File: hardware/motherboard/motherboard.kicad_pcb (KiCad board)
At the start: 4 copper layers, 150 x 90 mm, 32 parts, among them J1 Custom_PCIe_x4, J10 Conn_01x50_MountingPin, J11 Conn_01x50_MountingPin, J12 Barrel_Jack_Switch_Pin3Ring, J2 Custom_PCIe_x4, J3 Custom_PCIe_x4, J4 Custom_PCIe_x4, J5 Custom_PCIe_x4, J6 Custom_PCIe_x4, J7 Custom_PCIe_x4, J8 Custom_PCIe_x4, J9 Conn_01x50_MountingPin, U1 74HC138, U2 TMUX1208PW, U3 SN74LV595, U5 74HC138

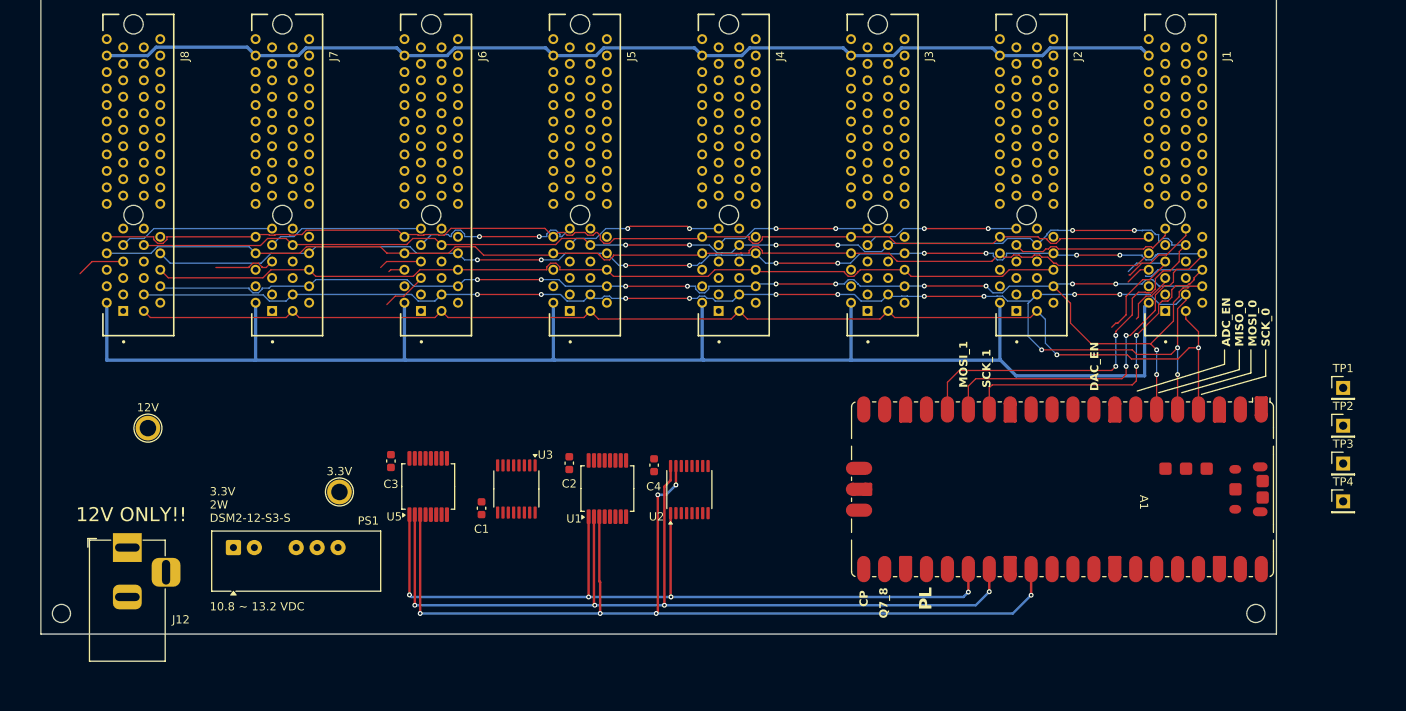
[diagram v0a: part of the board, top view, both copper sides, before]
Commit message: Motherboard: protected power input, K7805 switcher, working 3V3_EN interlock
Rework the motherboard power tree from the barrel jack to the 3.3 V rail.
Design rationale and verification are recorded in hardware/motherboard/POWER.md.

Input protection (new):
- F1 PPTC 1.5 A hold / 3 A trip (1812L150/24MR) -> D2 SMBJ13A TVS -> Q1 AO3407A
  P-FET reverse-polarity, in that order so a surge or reversed jack crowbars
  through the fuse.
- Q1 is drain-to-supply / source-to-load; source-to-supply passes reverse
  current through the body diode and fails silently.
- AO3407A (Vgs +/-20 V) replaces AO3401A (+/-12 V), which sat at its absolute
  maximum on a 12 V rail and needed a gate zener conducting continuously.
- +12 V now actually reaches J1-J8 pin A30; it was previously an orphan net
  with no source.

Regulation:
- U8 L7805 -> K7805-500R3 switching module, pin-compatible with LM78xx.
  Cuts 12->5 V loss from ~1.5 W to ~0.15 W. TRACO TSR-1 symbol/footprint match
  the datasheet layout (3 x 1.00 mm holes, 2.54 mm pitch).
- Datasheet-required caps added: C5 10 uF/50 V at the input, C6 22 uF at the
  output, C7 220 uF electrolytic bulk for load steps and hot-plug damping.

3V3_EN interlock (was inert):
- R7 100k -> 10k, R8 100k -> 4.7k with its far end moved from the Pico's own
  3V3 output (pin 36) to the board +3.3 V rail. As wired it was a bootstrap
  divider off the regulator's own output that enabled in every case.
- Verified against RT6150A/B DS6150A/B-06: EN logic-low max 0.4 V, logic-high
  min 1.2 V. Board rail dead -> 0.146 V (off); rail up -> 2.32 V (on).

Also:
- U1/U5 SN74LVC138APWR -> SN74HC138PWR: 8x cheaper, ~50k stock vs 669, and
  the decoders are static during a transfer (address then enable, then SPI).
  Footprint corrected SSOP-16 -> TSSOP-16, matching the PW part and U2/U3.
- Capacitors standardised on 0805 (C8 stays 1210 for DC-bias reasons).
- Footprints assigned to F1/R1/R6/R7/R8; LCSC part numbers recorded in POWER.md.
- .gitignore: padne output, Ki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
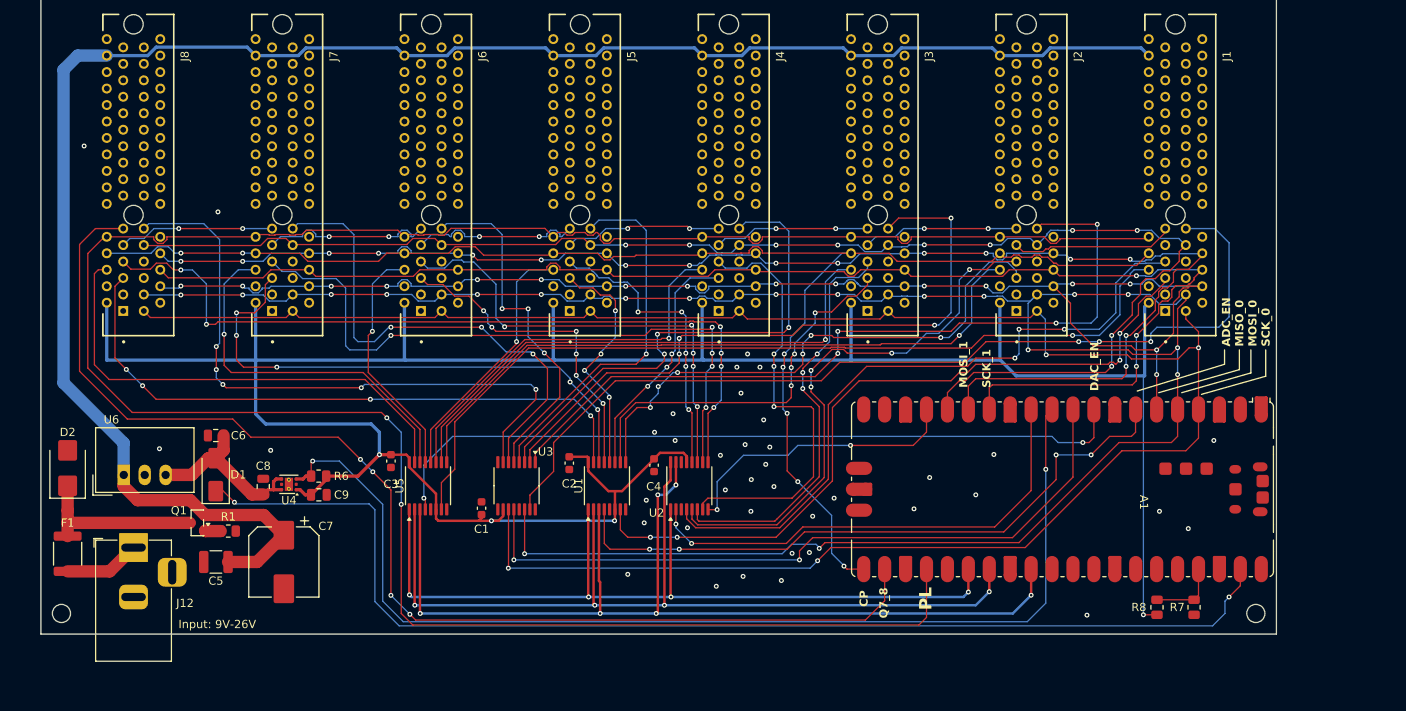
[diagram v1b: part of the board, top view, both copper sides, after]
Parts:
- removed 12V, 3.3V: TestPoint_Plated_Hole_D2.0mm, TestPoint:TestPoint_Plated_Hole_D2.0mm
- removed PS1: DSM2-12-S3-S, Converter_DCDC:Converter_DCDC_XP_POWER-IAxxxxS_THT
- removed TP1, TP2, TP3, TP4: TestPoint, Connector_PinHeader_2.54mm:PinHeader_1x01_P2.54mm_Vertical
- added C5: 10uF, Capacitor_SMD:C_1210_3225Metric, F.Cu at (103.8, 123.8)
- added C6: 22uF, Capacitor_SMD:C_0805_2012Metric, F.Cu at (103.7, 108.4)
- added C7: 220uF, Capacitor_SMD:CP_Elec_8x10, F.Cu at (112.0, 123.8)
- added C8: 10uF, Capacitor_SMD:C_0805_2012Metric, F.Cu at (109.5, 114.6)
- added C9: 10uF, Capacitor_SMD:C_0805_2012Metric, F.Cu at (116.2, 115.6)
- added D1: SS34, Diode_SMD:D_SMA, F.Cu at (103.7, 113.2)
- added D2: SMBJ13A, Diode_SMD:D_SMB, F.Cu at (85.8, 112.3)
- added F1: 1812L150/24MR, Fuse:Fuse_1812_4532Metric, F.Cu at (85.8, 122.8)
- added Q1: AO3407A, Package_TO_SOT_SMD:SOT-23, F.Cu at (101.5, 119.0)
- added R1: 100k, Resistor_SMD:R_0805_2012Metric, F.Cu at (105.2, 120.0)
- added R6: 100k, Resistor_SMD:R_0805_2012Metric, F.Cu at (116.2, 113.3)
- added R7: 10k, Resistor_SMD:R_0805_2012Metric, F.Cu at (222.5, 129.2)
- added R8: 4.7k, Resistor_SMD:R_0805_2012Metric, F.Cu at (218.0, 129.2)
- added U4: LP5912-3.3DRV, Package_SON:WSON-6-1EP_2x2mm_P0.65mm_EP1x1.6mm_ThermalVias, F.Cu at (112.6, 114.3)
- added U6: K7805-500R3, Converter_DCDC:Converter_DCDC_TRACO_TSR-1_THT, F.Cu at (92.6, 113.2)
- J1, J2, J3, J4, J5, J6, J7, J8: value Custom_PCIe_x4 -> PCIE-064-02-F-D-TH
- U1, U5: value 74HC138 -> SN74HC138PWR; footprint Package_SO:SSOP-16_5.3x6.2mm_P0.65mm -> Package_SO:TSSOP-16_4.4x5mm_P0.65mm
- moved J12 0.75 mm to (93.8, 122.0)
- moved U2 0.46 mm to (161.2, 114.5)
- moved U3 0.39 mm to (140.2, 114.5)
- moved U1 0.34 mm to (151.2, 114.5)
- moved U5 0.09 mm to (129.5, 114.5)
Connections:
- A1 pad 11: unconnected-(A1-GPIO8-Pad11) -> PG
- A1 pad 37: unconnected-(A1-3V3_EN-Pad37) -> 3V3_EN
- A1 pad 39: unconnected-(A1-VSYS-Pad39) -> VSYS
- J1 pad B31: GND -> PRSNT
- J12 pad 1: +12V -> VIN_JACK
- J2 pad B31: GND -> unconnected-(J2-~{PRSNT2}-PadB31)
- J4 pad B31: GND -> unconnected-(J4-~{PRSNT2}-PadB31)
- J5 pad B31: GND -> unconnected-(J5-~{PRSNT2}-PadB31)
- J6 pad B31: GND -> unconnected-(J6-~{PRSNT2}-PadB31)
- J7 pad B31: GND -> unconnected-(J7-~{PRSNT2}-PadB31)
- J8 pad B31: GND -> unconnected-(J8-~{PRSNT2}-PadB31)
- U1 pad 6: GND -> +3.3V
- U5 pad 6: GND -> +3.3V
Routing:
- net PL: track 133.7 -> 285.0 mm, vias 0 -> 2
- net Q7_8: track 0.00 -> 144.1 mm, vias 0 -> 4
- net VSYS: track 0.00 -> 142.6 mm, vias 0 -> 2
- net PG: track 0.00 -> 132.6 mm, vias 0 -> 2
- net +3.3V: track 184.9 -> 315.6 mm, vias 0 -> 4
- net XTR_OD_1: track 9.73 -> 113.2 mm, vias 0 -> 3
- net DAC_CS1: track 3.11 -> 106.0 mm, vias 0 -> 1
- net SCK_0: track 149.6 -> 251.2 mm, vias 2 -> 4
- net XTR_OD_2: track 0.00 -> 96.6 mm, vias 0 -> 4
- net MOSI_0: track 171.2 -> 266.5 mm, vias 13 -> 19
- net DAC_EN: track 0.00 -> 92.2 mm, vias 0 -> 2
- net AT8: track 5.86 -> 96.6 mm, vias 0 -> 6
- net +12V: track 132.0 -> 221.6 mm
- net XTR_RCLK: track 0.00 -> 87.0 mm, vias 0 -> 2
- net ADC_CS1: track 6.80 -> 89.9 mm, vias 0 -> 4
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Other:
- board text added: "Input: 9V-26V"
- board text removed: "10.8 ~ 13.2 VDC"
- board text removed: "12V ONLY!!"
- board text removed: "3.3V 2W DSM2-12-S3-S"

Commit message: OPA2333 sense buffers and XTR200 EF fault-detection chain
Two daughterboard revisions plus the firmware to drive them.

OPA2333 sense buffers (root-causes the 3 mV offset):
- The ~3 mV offset seen during the 8-board test was the AD7193's *internal*
  input buffer. With the 6:1 divider, a low-current channel's ADC input sits
  below the buffered mode's usable common-mode range, so the buffer added a
  systematic offset instead of tracking.
- Fixed by disabling it (CONF.BUF = 0) and adding 8 external unity-gain
  followers: U13-U16 (OPA2333, 2 ch per package) between the divider taps and
  the ADC inputs, with R28-R35 1k series and C26-C33 100nF anti-alias
  (corner 1.59 kHz; was 339 kHz at 100R/4.7nF, which attenuated neither the
  OPA333 chop nor the AD7193 modulator rate).

XTR200 EF fault detection:
- Each daughterboard's SN74LV165 (U8) samples its eight XTR200 EF pins; the
  motherboard daisy-chains all eight into one 64-bit register on a private
  bit-banged 3-wire bus (CP=GP16, Q7=GP17, PL=GP18), so reading it never
  disturbs SPI0 (ADC + '595) or SPI1 (DAC).
- New EFChain.cpp/.h; loop() polls every 20 ms, latches a new fault, zeroes
  that channel's DAC and pins it at 0 mA until FAULTCLR.
- New host commands: FAULT?, FAULTCLR, FAULTEN ON|OFF.
- Documented limits: EF is one shared flag (open / saturation / SET short /
  UVLO <8 V / >150 C); open detection only arms above IOUT ~0.75 mA with
  RSET = 4.7k; an unpopulated slot breaks the chain, so efValidMask() reports
  which boards' bits are trustworthy.

Also:
- master_bom_lcsc.csv: U13-U16 and R28-R35 rows added (both LCSC-TBD), 100nF
  line 160 -> 224 units for C26-C33. Total understated until the OPA2333 line
  is priced.
- README: 3 mV offset moved from open issue to resolved.
- motherboard.kicad_pcb: 64 further routed segments.
- padne_plots_layers.py: per-layer padne plotting helper.
- paper/todo.txt: working notes.

Co-Authored-By: Claude Opus 5 <noreply@anthropic.com>
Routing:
- net CH7: track 0.00 -> 6.50 mm
- net CH63: track 0.00 -> 6.50 mm
- net CH62: track 0.00 -> 6.50 mm
- net CH61: track 0.00 -> 6.50 mm
- net CH60: track 0.00 -> 6.50 mm
- net CH6: track 0.00 -> 6.50 mm
- net CH59: track 0.00 -> 6.50 mm
- net CH58: track 0.00 -> 6.50 mm
- net CH55: track 0.00 -> 6.50 mm
- net CH54: track 0.00 -> 6.50 mm
- net CH53: track 0.00 -> 6.50 mm
- net CH52: track 0.00 -> 6.50 mm
- net CH51: track 0.00 -> 6.50 mm
- net CH50: track 0.00 -> 6.50 mm
- net CH5: track 0.00 -> 6.50 mm
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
